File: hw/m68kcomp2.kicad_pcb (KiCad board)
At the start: 4 copper layers, 248.9 x 167.6 mm, 113 parts, among them J1 SWRST, J2 CFMASTER, J3 AVR-ISP, J4 ACTLED, J5 ATX-24, J6 VREG_3V3, SW1 SWRST, SW2 SWPWR, U1 GAL20V8, U10 mc68881, U11 74HC393, U12 ATmega328PB-A, U13 cfconn, U14 ATA0, U15 mouse, U16 kbd, U17 ds1501, U18 mc68681, U19 74LVC125, U2 GAL16V8, U20 mc1489, U21 mc1488, U22 mc1488, U23 sdcard, U24 sera, U25 serb, U26 28C256, U27 as6c8008, U28 as6c8008, U29 as6c8008, U3 NE555D, U30 as6c8008, U31 exp_conn, U32 exp_conn, U33 LM1117-3.3, U4 74HC10, U5 74LS14, U6 74HC148, U7 74HC138, U8 mc68030rc, U9 GAL16V8, X1 25.175MHz, Y1 3.6864MHz, Y2 32.768kHz

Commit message: more pcb layout
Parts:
- moved U31 287.6 mm to (75.7, 67.0)
- moved U32 281.5 mm to (95.7, 67.0)
- moved BT1 139.1 mm to (227.9, -23.0)
- moved U17 139.1 mm to (198.0, -25.4)
- moved U21 39.5 mm to (180.5, 45.1)
- moved U20 16.6 mm to (168.0, 45.1)
- moved U22 16.6 mm to (155.4, 45.1)
- moved U10 16.4 mm to (293.1, 104.3)
- moved U15 16.4 mm to (250.1, 25.3)
- moved U16 16.4 mm to (270.4, 25.3)
- moved U18 16.4 mm to (115.8, 72.5)
- moved U19 16.4 mm to (297.9, 144.4)
- moved U24 16.4 mm to (225.2, 36.0)
- moved U25 16.4 mm to (189.6, 36.0)
- moved U26 16.4 mm to (137.3, 87.8)
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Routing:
- net /io/RXDA: track 0.00 -> 117.2 mm
- net /io/RTRA: track 1.27 -> 110.7 mm
- net /io/RTRB: track 0.00 -> 102.2 mm
- net /io/TXDA: track 0.00 -> 98.9 mm
- net /io/TXDB: track 0.00 -> 96.2 mm
- net /io/RXDB: track 0.00 -> 78.8 mm
- net A3: track 271.4 -> 342.0 mm
- net A2: track 280.9 -> 344.9 mm, vias 8 -> 9
- net A4: track 258.9 -> 321.7 mm, vias 8 -> 9
- net A5: track 225.2 -> 282.3 mm
- net /io/DTRB: track 49.1 -> 88.6 mm
- net /io/RTRA_232: track 21.2 -> 50.8 mm
- net /io/TXDB_232: track 57.3 -> 29.7 mm
- net /io/TXDA_232: track 25.0 -> 0.00 mm
- net -12V: track 0.00 -> 24.2 mm
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
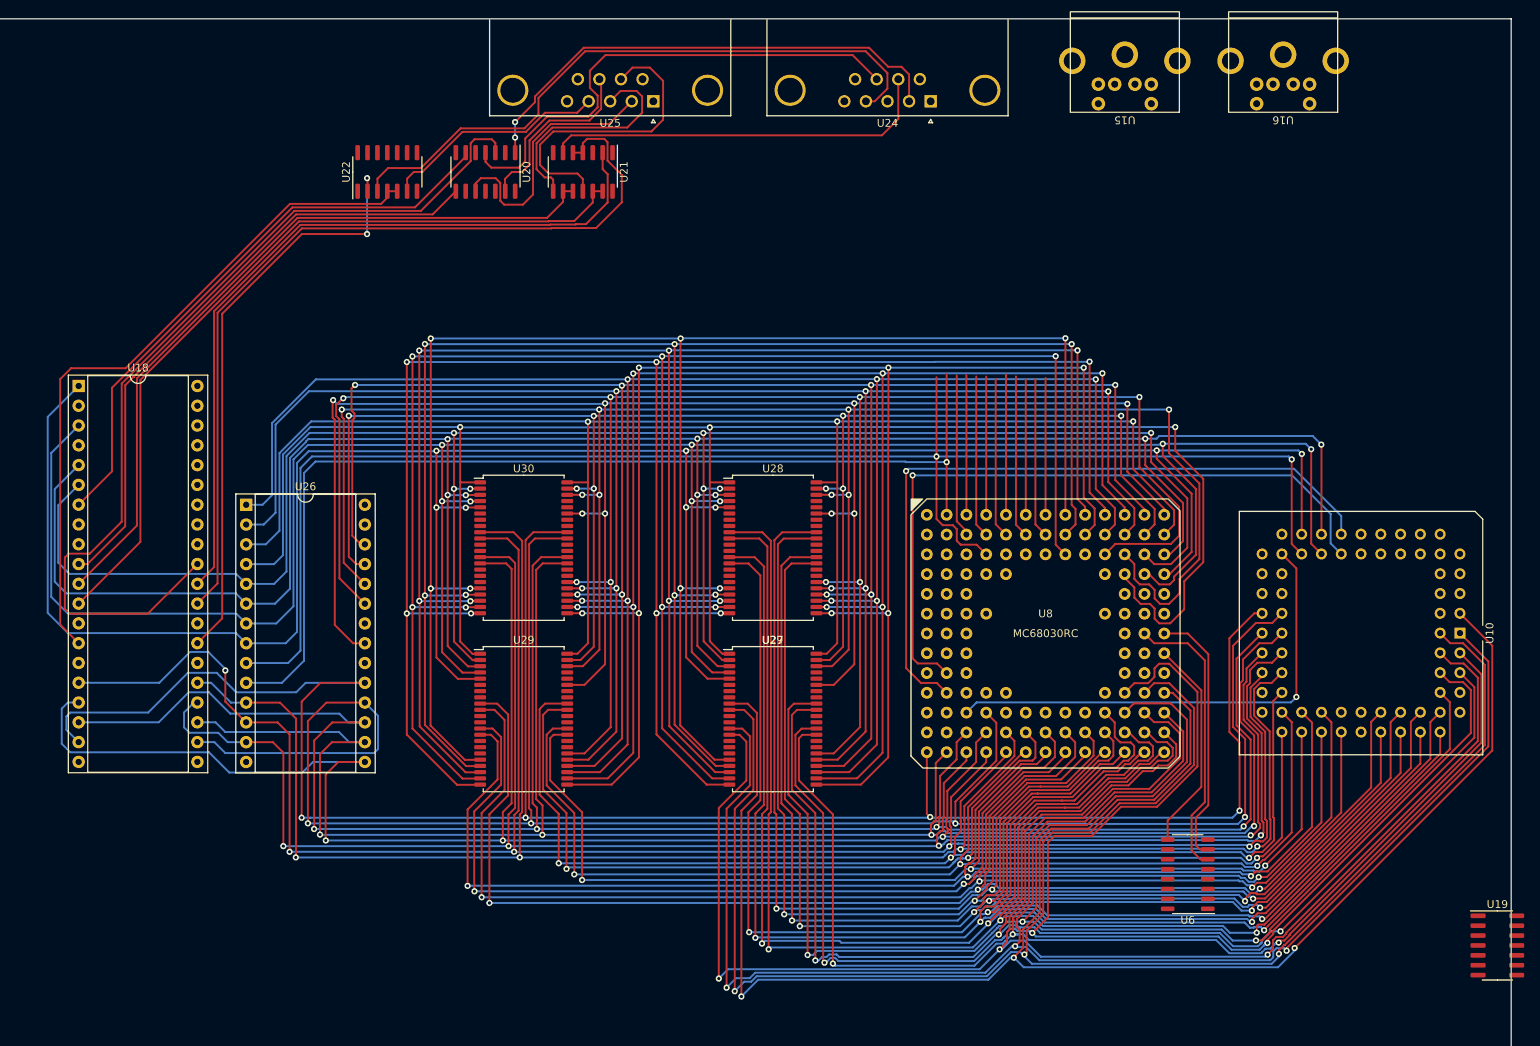
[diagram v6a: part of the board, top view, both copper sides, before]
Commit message: cleaned up some of the bus traces
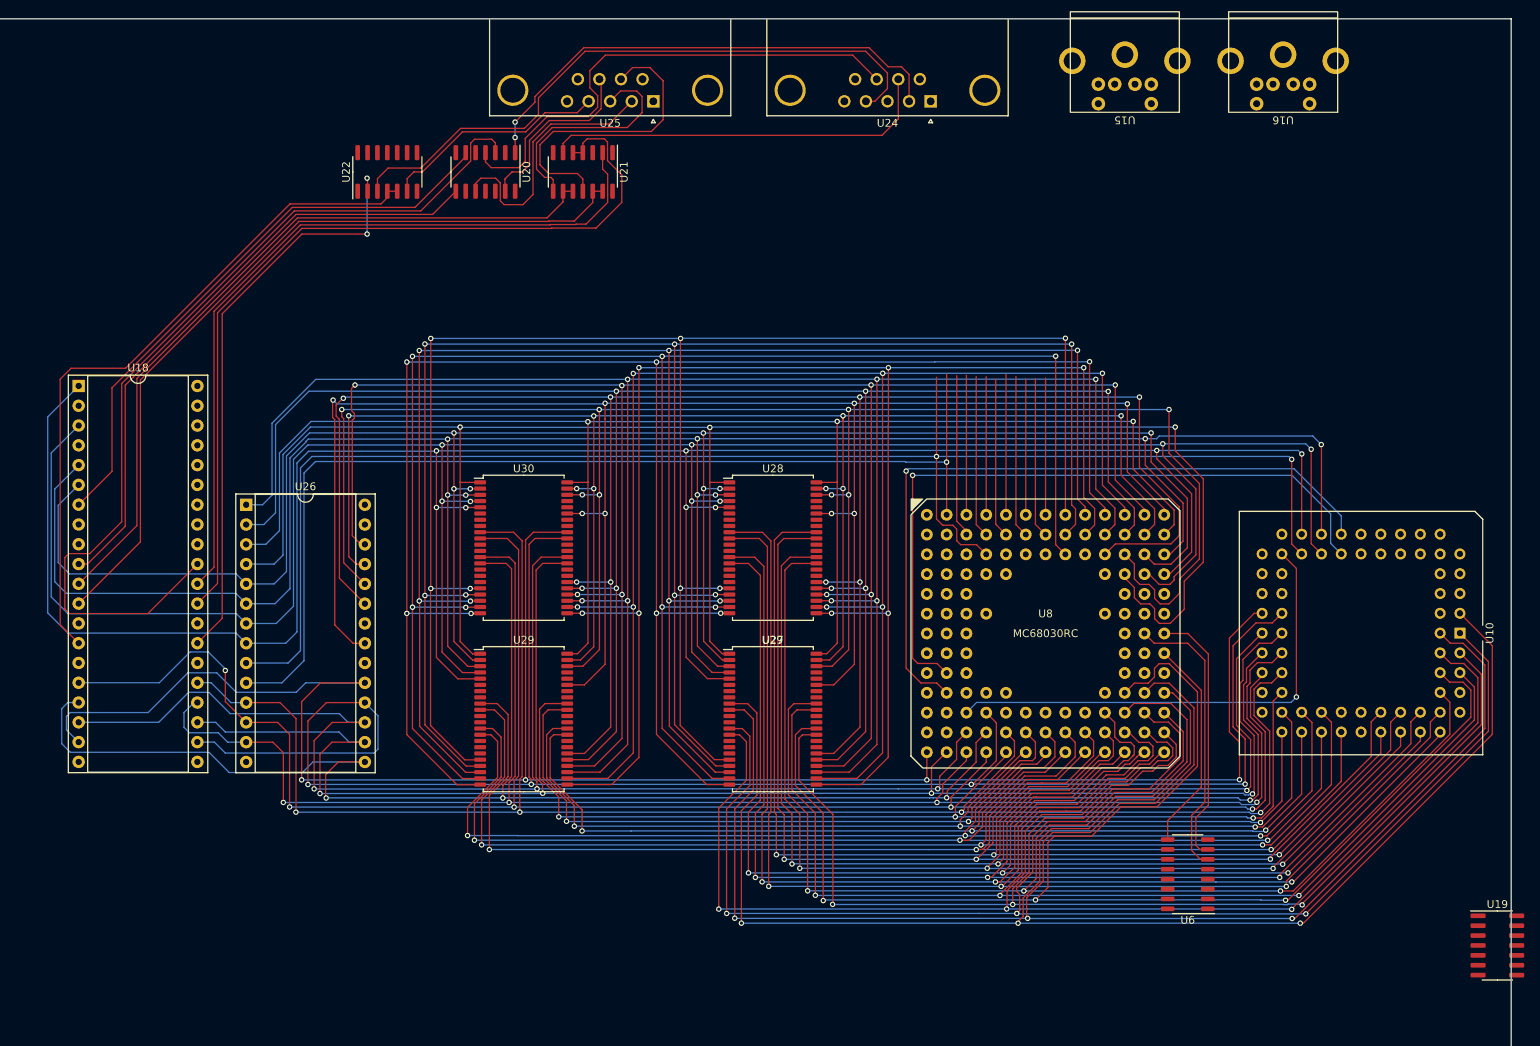
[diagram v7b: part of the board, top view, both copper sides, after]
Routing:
- net D25: track 279.4 -> 256.9 mm
- net D26: track 259.8 -> 237.6 mm
- net D24: track 269.1 -> 247.1 mm
- net D3: track 225.6 -> 203.7 mm
- net D2: track 232.2 -> 211.0 mm
- net D27: track 283.3 -> 262.2 mm
- net D1: track 243.6 -> 222.5 mm
- net D6: track 208.8 -> 187.7 mm
- net D28: track 259.6 -> 238.8 mm
- net D10: track 218.7 -> 198.0 mm
- net D12: track 200.6 -> 180.0 mm
- net D30: track 282.5 -> 261.9 mm
- net D0: track 243.0 -> 222.6 mm
- net D9: track 220.6 -> 200.4 mm
- net D11: track 206.5 -> 186.4 mm
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
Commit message: more pcb layout
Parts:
- moved U14 396.8 mm to (148.8, 138.9), turned to 90 degrees
- moved X1 326.5 mm to (212.3, 60.3), turned to -90 degrees
- moved U13 281.2 mm to (87.1, 117.2)
- moved U11 261.3 mm to (194.7, 195.2)
- moved BT1 239.4 mm to (26.8, 106.8)
- moved U9 186.2 mm to (170.6, 183.6)
- moved U12 129.8 mm to (250.1, 48.2), turned to -90 degrees
- moved U17 111.4 mm to (116.0, 50.0)
- moved J3 106.4 mm to (234.5, 44.4), turned to -90 degrees
- moved U1 42.0 mm to (11.1, 128.3)
- moved J5 35.1 mm to (287.1, 79.6)
- moved U23 23.8 mm to (318.0, 208.3)
- moved U6 7.25 mm to (260.4, 128.3)
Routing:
- net D29: track 259.4 -> 324.0 mm, vias 4 -> 5
- net D30: track 261.9 -> 305.0 mm, vias 5 -> 6
- net D31: track 270.8 -> 313.3 mm, vias 4 -> 6
- net ~{RESET}: track 21.2 -> 50.6 mm, vias 1 -> 3
- net D20: track 158.2 -> 184.7 mm, vias 4 -> 5
- net /io/KBDATA: track 0.00 -> 25.0 mm
- net D25: track 256.9 -> 281.6 mm, vias 5 -> 6
- net D21: track 155.3 -> 178.1 mm, vias 3 -> 4
- net /io/SCK: track 0.00 -> 22.5 mm
- net D16: track 183.6 -> 205.5 mm, vias 4 -> 5
- net A14: track 291.2 -> 270.1 mm
- net /io/MOSI: track 0.00 -> 20.4 mm
- net D22: track 157.4 -> 177.6 mm, vias 4 -> 5
- net D26: track 237.6 -> 256.2 mm
- net A12: track 281.1 -> 262.7 mm
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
